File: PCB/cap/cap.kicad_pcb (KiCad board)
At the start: 2 copper layers, 45 x 65 mm, 24 parts, among them J1 Servo1, J3 LS1, J4 LS2, J5 VCC/GND-IN, J7 FSR1, U1 ACS723xLCTR-05AB, U2 NRF24L01_Breakout, U3 INA181A3

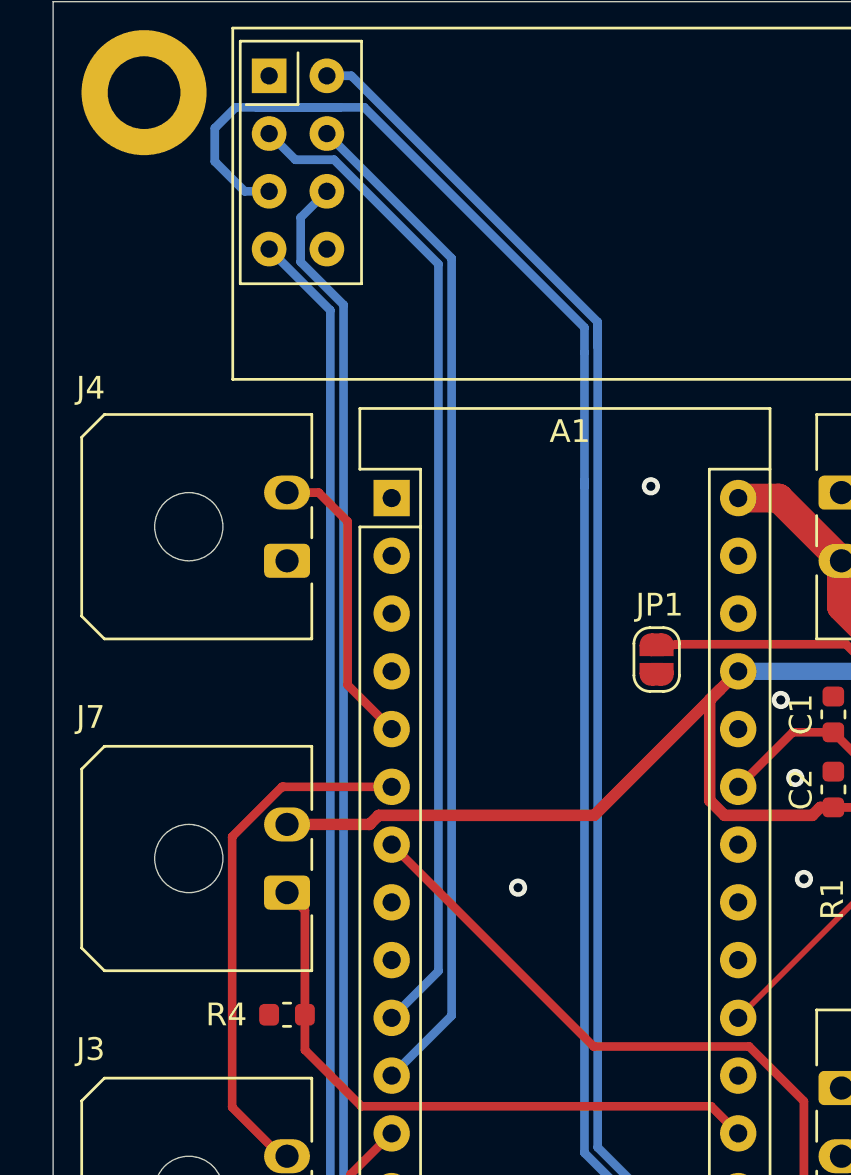
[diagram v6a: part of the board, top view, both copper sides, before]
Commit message: Completed camera layout
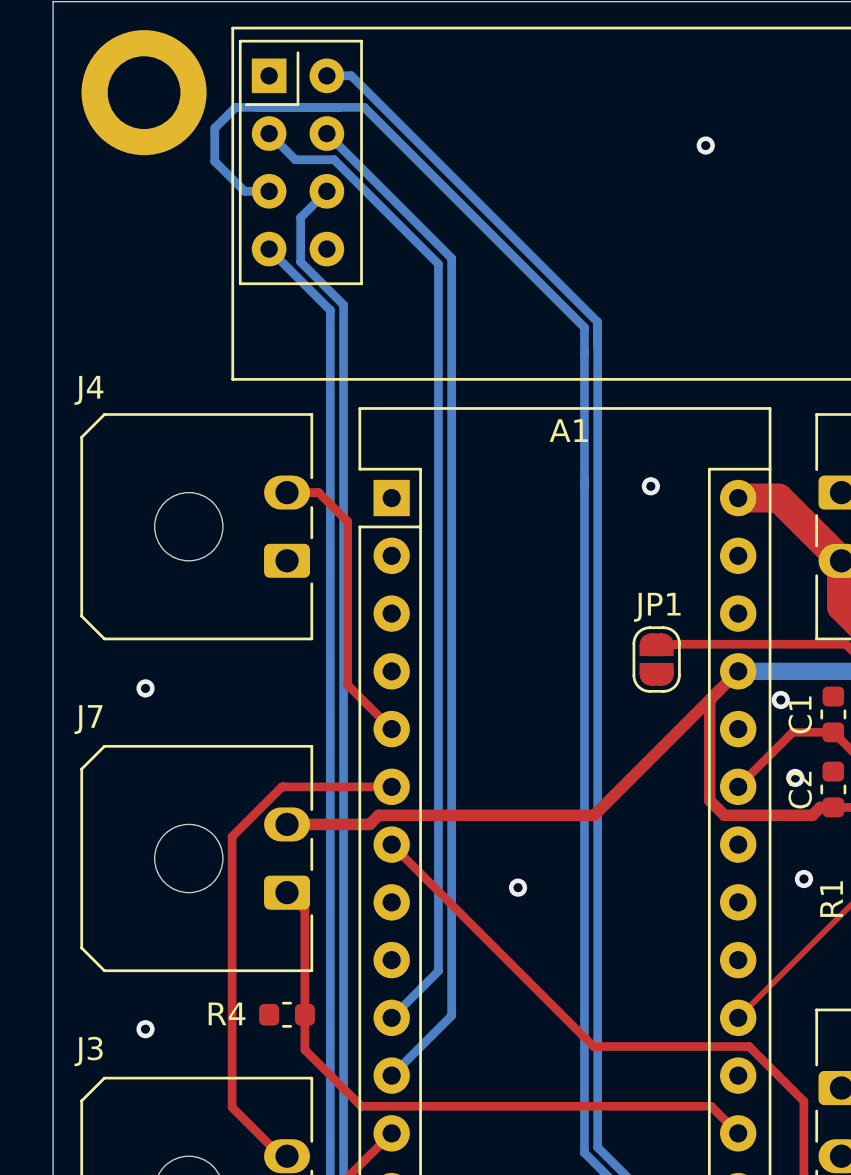
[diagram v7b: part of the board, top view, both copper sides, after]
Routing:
- net GND: vias 5 -> 8
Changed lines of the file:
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@@
-(kicad_pcb (version 20171130) (host pcbnew "(5.1.4-0-10_14)")
+(kicad_pcb (version 20171130) (host pcbnew "(5.1.5)-3")
   (general
     (thickness 1.6)
-    (drawings 9)
-    (tracks 155)
+    (drawings 8)
+    (tracks 158)
     (zones 0)
     (modules 24)
@@
   )
   (setup
-    (last_trace_width 0.762)
+    (last_trace_width 0.381)
     (user_trace_width 0.254)
     (user_trace_width 0.508)
@@
     )
   )
-  (dimension 5.656912 (width 0.15) (layer F.Fab)
-    (gr_text "5.657 mm" (at 112.924011 108.932446 44.74217073) (layer F.Fab)
-      (effects (font (size 1 1) (thickness 0.15)))
-    )
-    (feature1 (pts (xy 109.982 109.982) (xy 110.41271 110.416604)))
-    (feature2 (pts (xy 114 106) (xy 114.43071 106.434604)))
-    (crossbar (pts (xy 114.017918 106.01808) (xy 109.999918 110.00008)))
-    (arrow1a (pts (xy 109.999918 110.00008) (xy 110.387261 108.79059)))
-    (arrow1b (pts (xy 109.999918 110.00008) (xy 111.212845 109.623638)))
-    (arrow2a (pts (xy 114.017918 106.01808) (xy 112.804991 106.394522)))
-    (arrow2b (pts (xy 114.017918 106.01808) (xy 113.630575 107.22757)))
-  )
   (dimension 57 (width 0.15) (layer F.Fab)
     (gr_text "57.000 mm" (at 101.824 77.5 90) (layer F.Fab)
@@
   (segment (start 150.3235 86.819) (end 150.77899 86.36351) (width 0.762) (layer F.Cu) (net 3))
   (segment (start 150.3235 87.394) (end 150.3235 86.819) (width 0.762) (layer F.Cu) (net 3))
+  (via (at 114.064 75.202) (size 0.8) (drill 0.4) (layers F.Cu B.Cu) (net 3))
+  (via (at 114.064 90.188) (size 0.8) (drill 0.4) (layers F.Cu B.Cu) (net 3))
+  (via (at 138.702 51.326) (size 0.8) (drill 0.4) (layers F.Cu B.Cu) (net 3))
   (segment (start 143.415 108.22) (end 143.415 106.317) (width 0.381) (layer F.Cu) (net 4) (status 30))
   (segment (start 120.027 95.776) (end 117.874 93.623) (width 0.381) (layer F.Cu) (net 5))

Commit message: Cap review complete. Create gerbers
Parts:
- D1: value G-LED -> R-LED
- R2, R5: value - -> 220 ohm
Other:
- board text added: "FSR"
- board text added: "SW-1"
- board text added: "SW-2"
- board text added: "V1.0"
- board text added: "Vin"
